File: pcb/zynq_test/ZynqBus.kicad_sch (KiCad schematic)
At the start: 1 part, among them U1 XC7Z020-2CLG400I

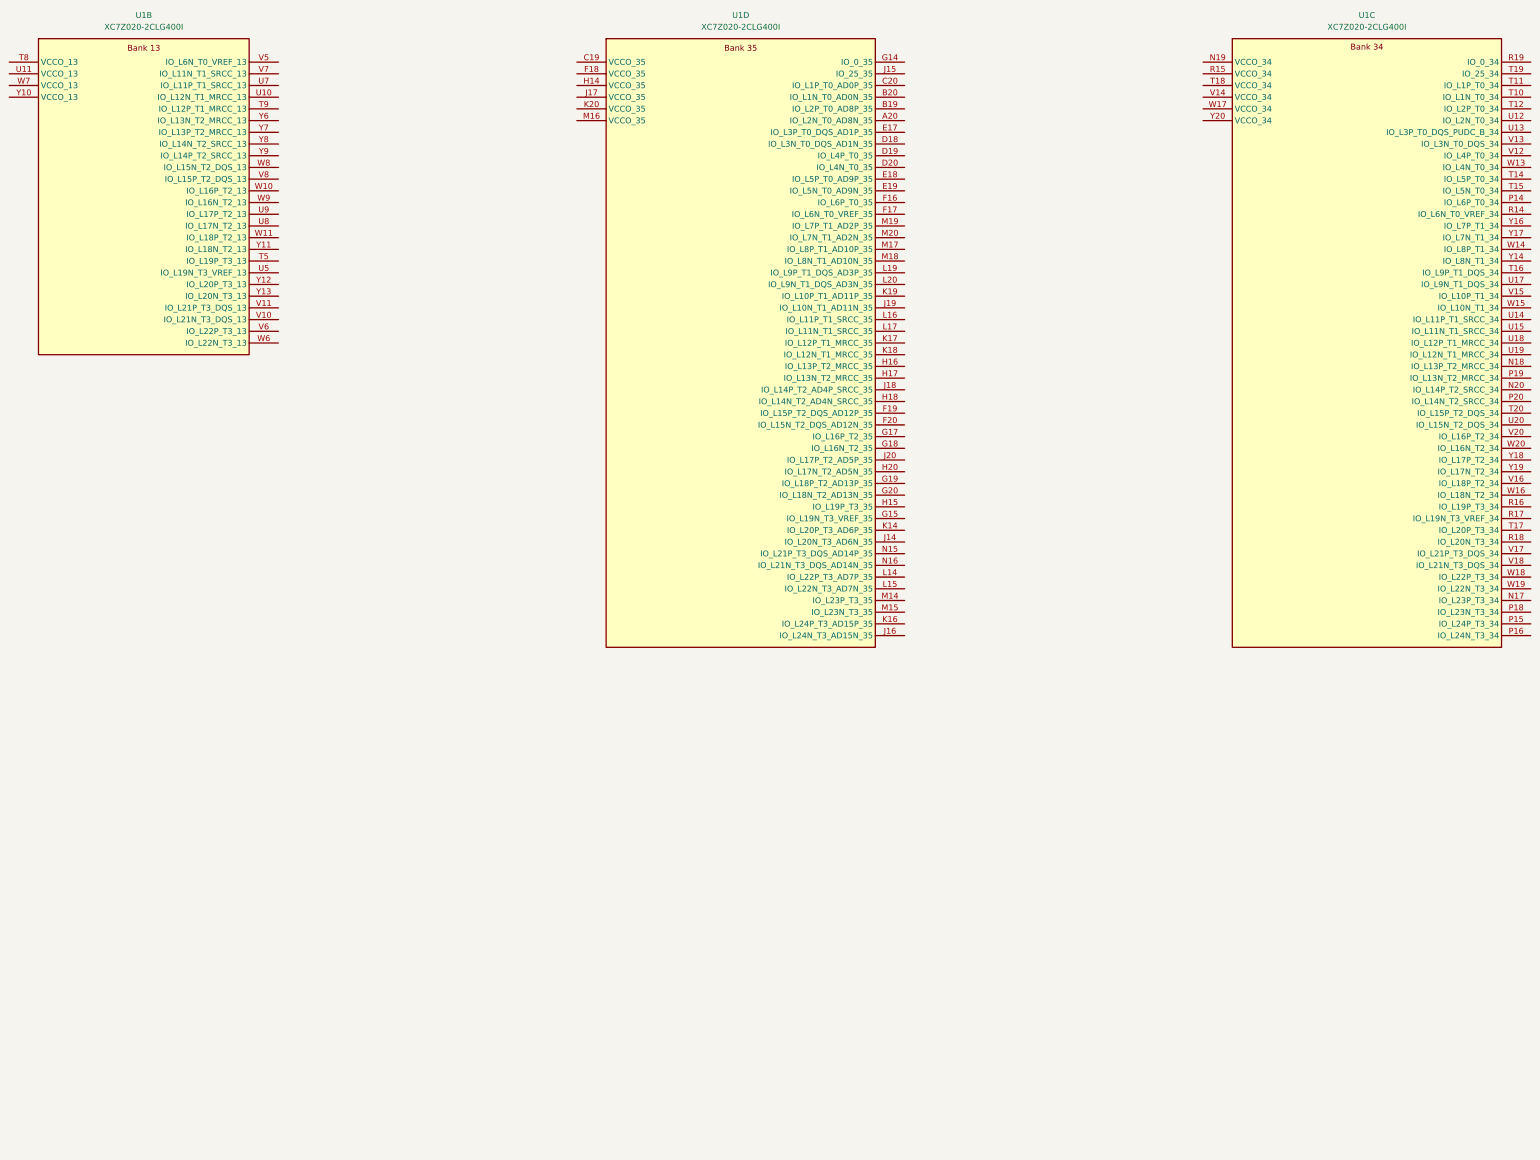
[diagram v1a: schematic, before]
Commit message: Finished PS, started on PWR
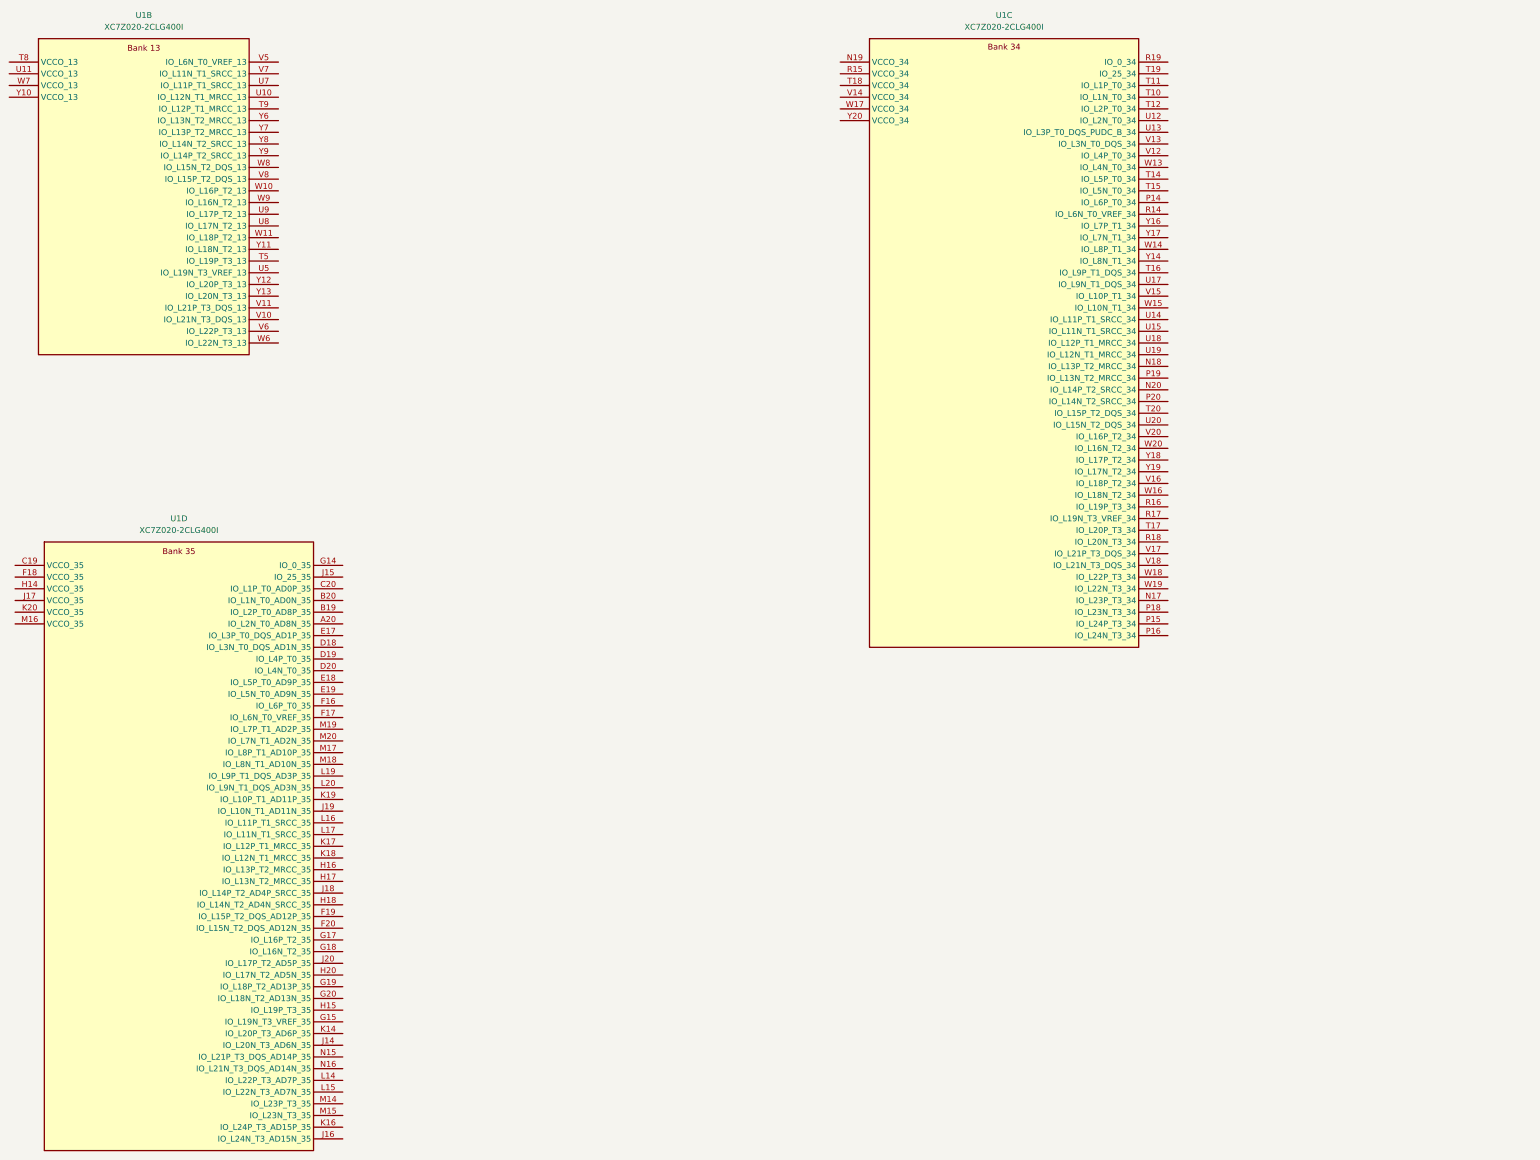
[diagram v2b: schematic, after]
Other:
- moved on the sheet: U1C, U1D
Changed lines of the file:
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@@
 	(symbol
 		(lib_id "zynq:XC7Z020-2CLG400I")
-		(at 199.39 92.71 0)
+		(at 77.47 201.93 0)
 		(unit 4)
 		(exclude_from_sim no)
@@
 		(fields_autoplaced yes)
 		(property "Reference" "U1"
-			(at 199.39 21.59 0)
+			(at 77.47 130.81 0)
 			(effects
 				(font
@@
 		)
 		(property "Value" "XC7Z020-2CLG400I"
-			(at 199.39 24.13 0)
+			(at 77.47 133.35 0)
 			(effects
 				(font
@@
 		)
 		(property "Footprint" "Zynq:CLG400_ZYNQ-7000_AMD"
-			(at 170.18 16.51 0)
+			(at 48.26 125.73 0)
 			(effects
 				(font
@@
 		)
 		(property "Datasheet" ""
-			(at 170.18 16.51 0)
+			(at 48.26 125.73 0)
 			(effects
 				(font
@@
 		)
 		(property "Description" ""
-			(at 170.18 16.51 0)
+			(at 48.26 125.73 0)
 			(effects
 				(font
@@
 	(symbol
 		(lib_id "zynq:XC7Z020-2CLG400I")
-		(at 335.28 92.71 0)
+		(at 256.54 92.71 0)
 		(unit 3)
 		(exclude_from_sim no)
@@
 		(fields_autoplaced yes)
 		(property "Reference" "U1"
-			(at 335.28 21.59 0)
+			(at 256.54 21.59 0)
 			(effects
 				(font
@@
 		)
 		(property "Value" "XC7Z020-2CLG400I"
-			(at 335.28 24.13 0)
+			(at 256.54 24.13 0)
 			(effects
 				(font
@@
 		)
 		(property "Footprint" "Zynq:CLG400_ZYNQ-7000_AMD"
-			(at 306.07 16.51 0)
+			(at 227.33 16.51 0)
 			(effects
 				(font
@@
 		)
 		(property "Datasheet" ""
-			(at 306.07 16.51 0)
+			(at 227.33 16.51 0)
 			(effects
 				(font
@@
 		)
 		(property "Description" ""
-			(at 306.07 16.51 0)
+			(at 227.33 16.51 0)
 			(effects
 				(font

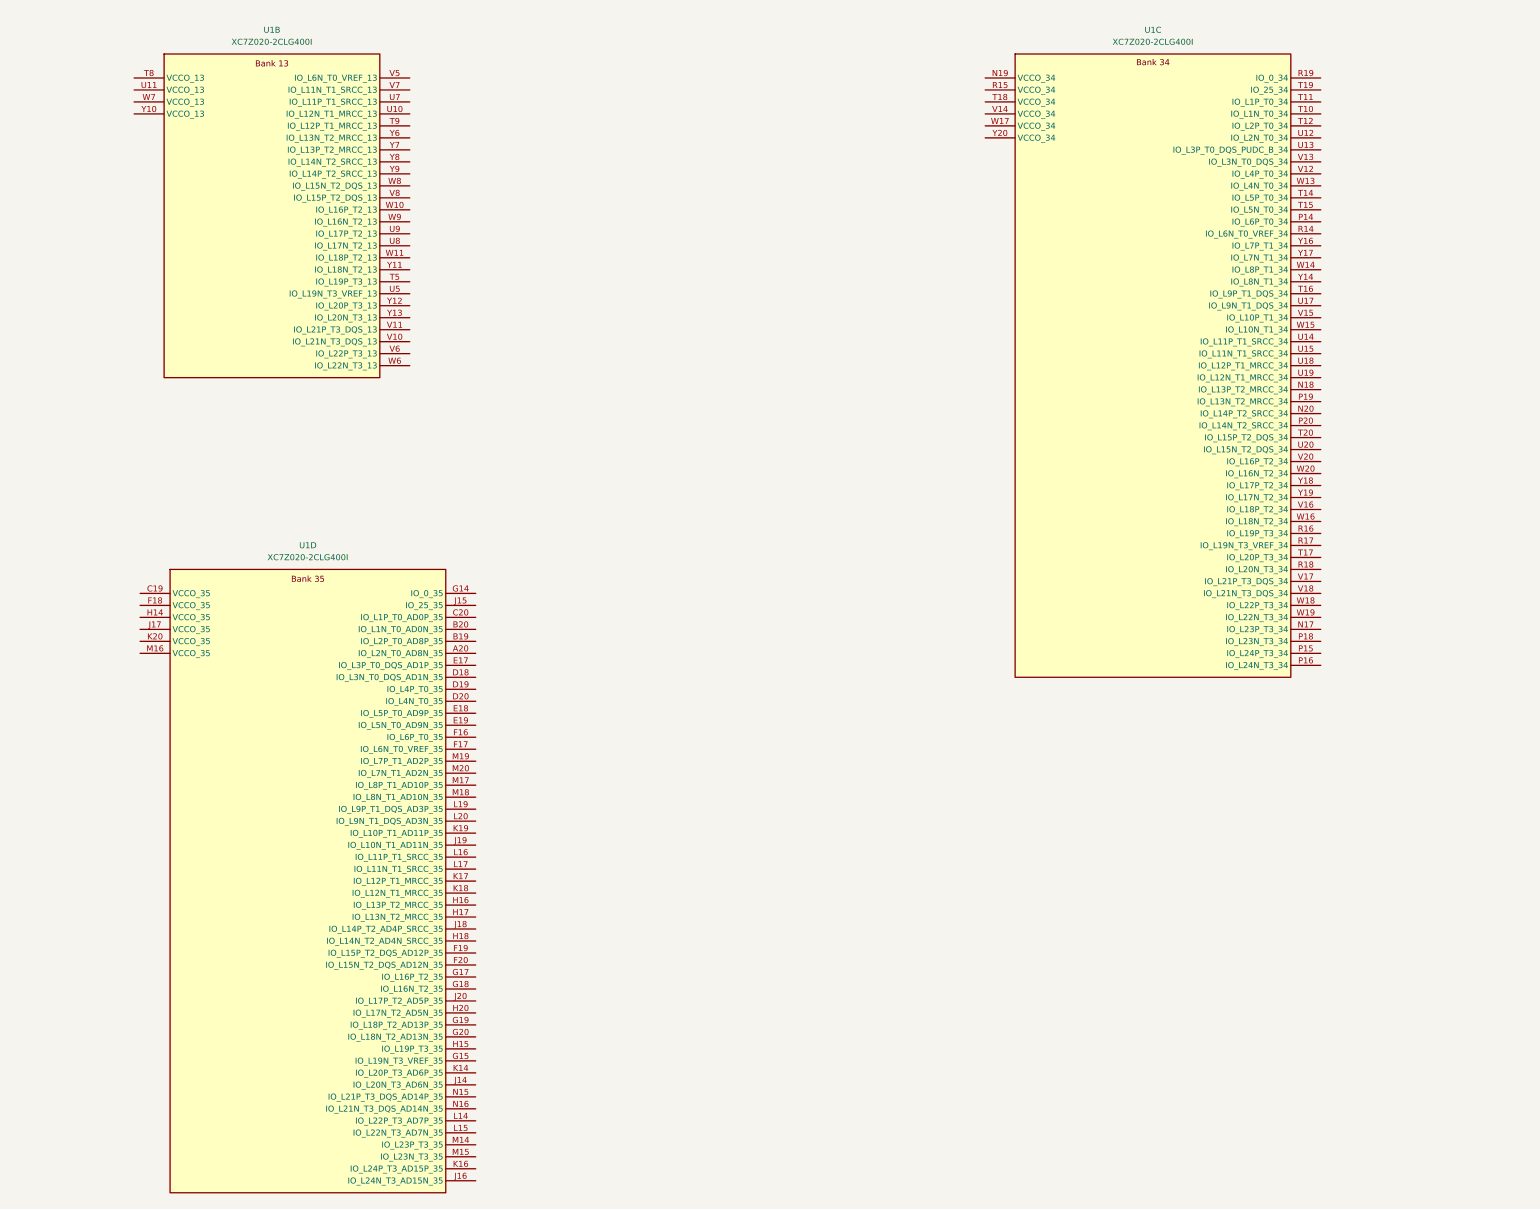
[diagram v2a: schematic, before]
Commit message: Finished FPGA decouploing, and jtag programmer
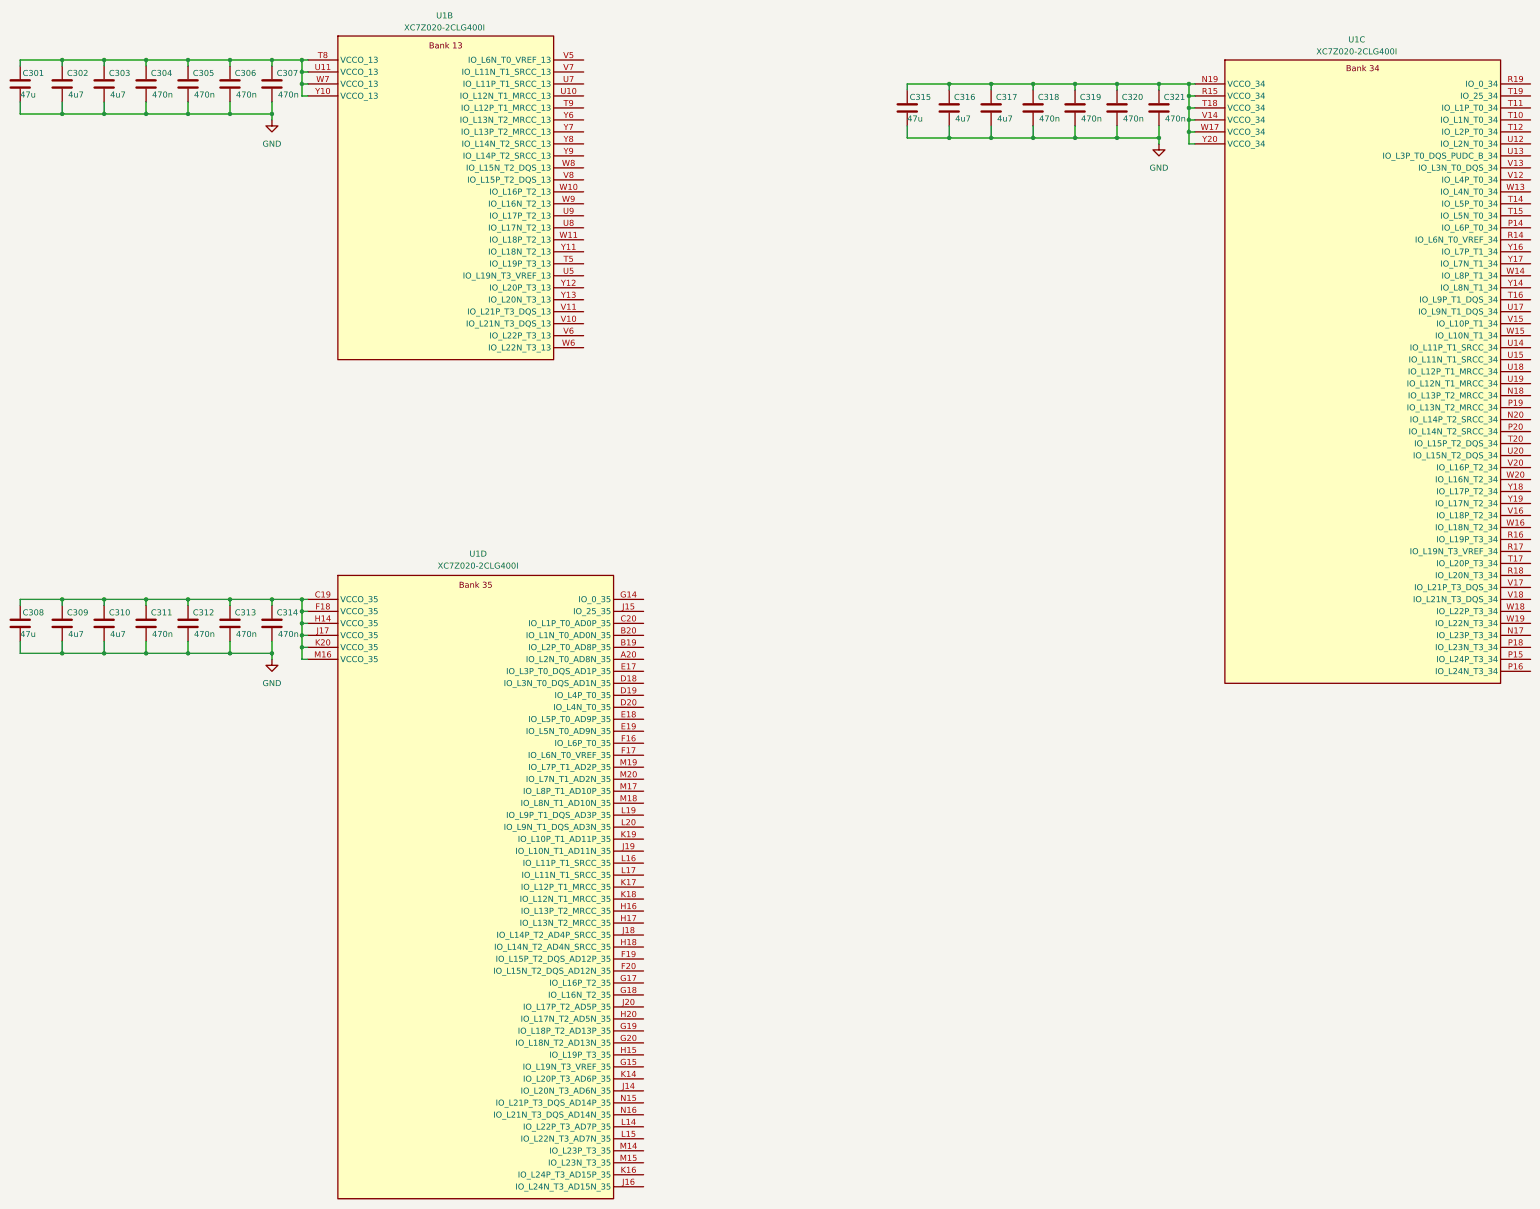
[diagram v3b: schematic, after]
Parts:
- added C301, C308, C315: 47u, symbol Device:C
- added C302, C303, C309, C310, C316, C317: 4u7, symbol Device:C
- added C304, C305, C306, C307, C311, C312, C313, C314, C318, C319, C320, C321: 470n, symbol Device:C
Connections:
- net at U1.T8 (VCCO_13): now also U1.U11 (VCCO_13), U1.W7 (VCCO_13), U1.Y10 (VCCO_13), C301.1, C302.1, C303.1, C304.1, C305.1, C306.1, C307.1
- net at U1.C19 (VCCO_35): now also U1.F18 (VCCO_35), U1.H14 (VCCO_35), U1.J17 (VCCO_35), U1.K20 (VCCO_35), U1.M16 (VCCO_35), C308.1, C309.1, C310.1, C311.1, C312.1, C313.1, C314.1
- net at U1.N19 (VCCO_34): now also U1.R15 (VCCO_34), U1.T18 (VCCO_34), U1.V14 (VCCO_34), U1.W17 (VCCO_34), U1.Y20 (VCCO_34), C315.1, C316.1, C317.1, C318.1, C319.1, C320.1, C321.1
- new net GND: C301.2, C302.2, C303.2, C304.2, C305.2, C306.2, C307.2, C308.2, C309.2, C310.2, C311.2, C312.2, C313.2, C314.2, C315.2, C316.2, C317.2, C318.2, C319.2, C320.2, C321.2
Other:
- moved on the sheet: U1B, U1C, U1D

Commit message: Finished HDMI
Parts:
- U1: footprint Zynq:CLG400_ZYNQ-7000_AMD -> Package_BGA:Xilinx_CLG400
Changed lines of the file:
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@@
 			)
 		)
-		(property "Footprint" "Zynq:CLG400_ZYNQ-7000_AMD"
+		(property "Footprint" "Package_BGA:Xilinx_CLG400"
 			(at 77.47 -17.78 0)
 			(effects
@@
 			)
 		)
-		(property "Footprint" "Zynq:CLG400_ZYNQ-7000_AMD"
+		(property "Footprint" "Package_BGA:Xilinx_CLG400"
 			(at 83.82 127 0)
 			(effects
@@
 			)
 		)
-		(property "Footprint" "Zynq:CLG400_ZYNQ-7000_AMD"
+		(property "Footprint" "Package_BGA:Xilinx_CLG400"
 			(at 271.78 17.78 0)
 			(effects
